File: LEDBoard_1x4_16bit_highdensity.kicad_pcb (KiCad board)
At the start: 2 copper layers, 16 x 14 mm, 10 parts, among them J1 signal_in, J2 signal_out, J3 power, U1 TLC5971PWP

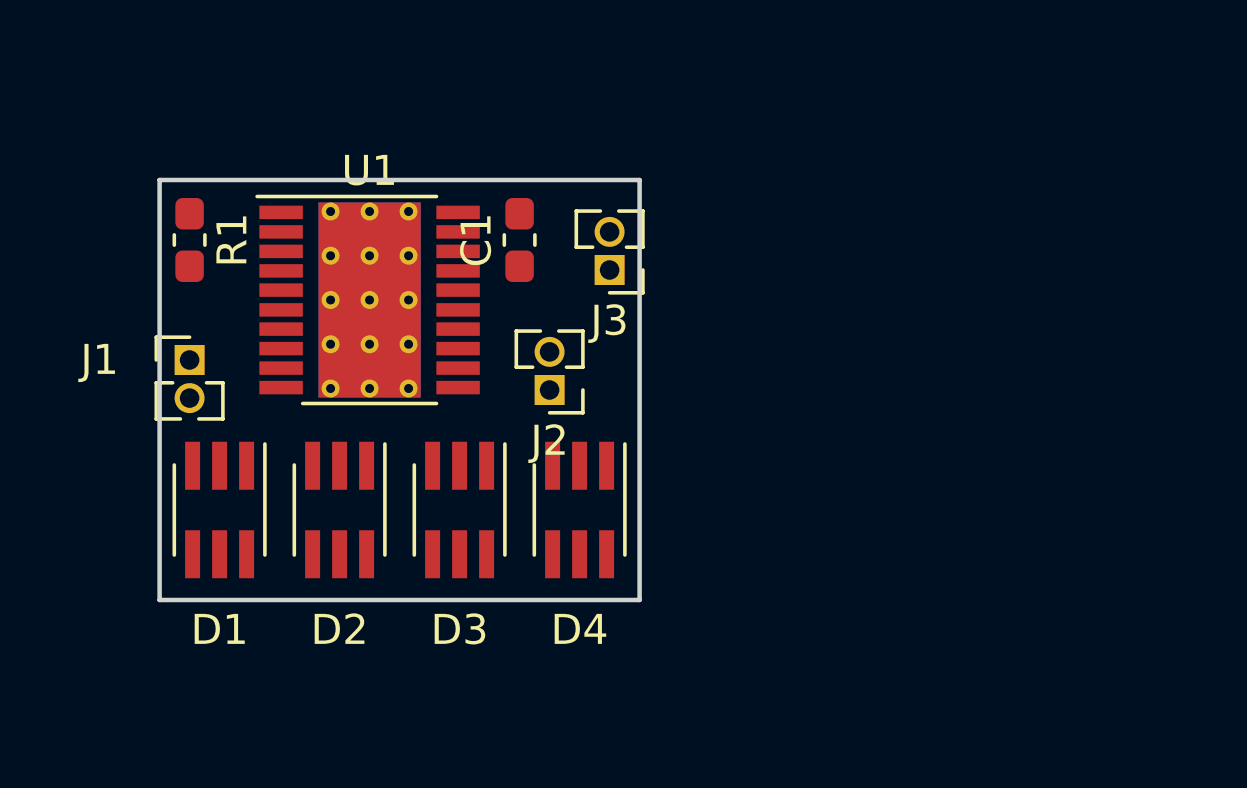
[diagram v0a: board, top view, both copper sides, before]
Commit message: basic component placement done
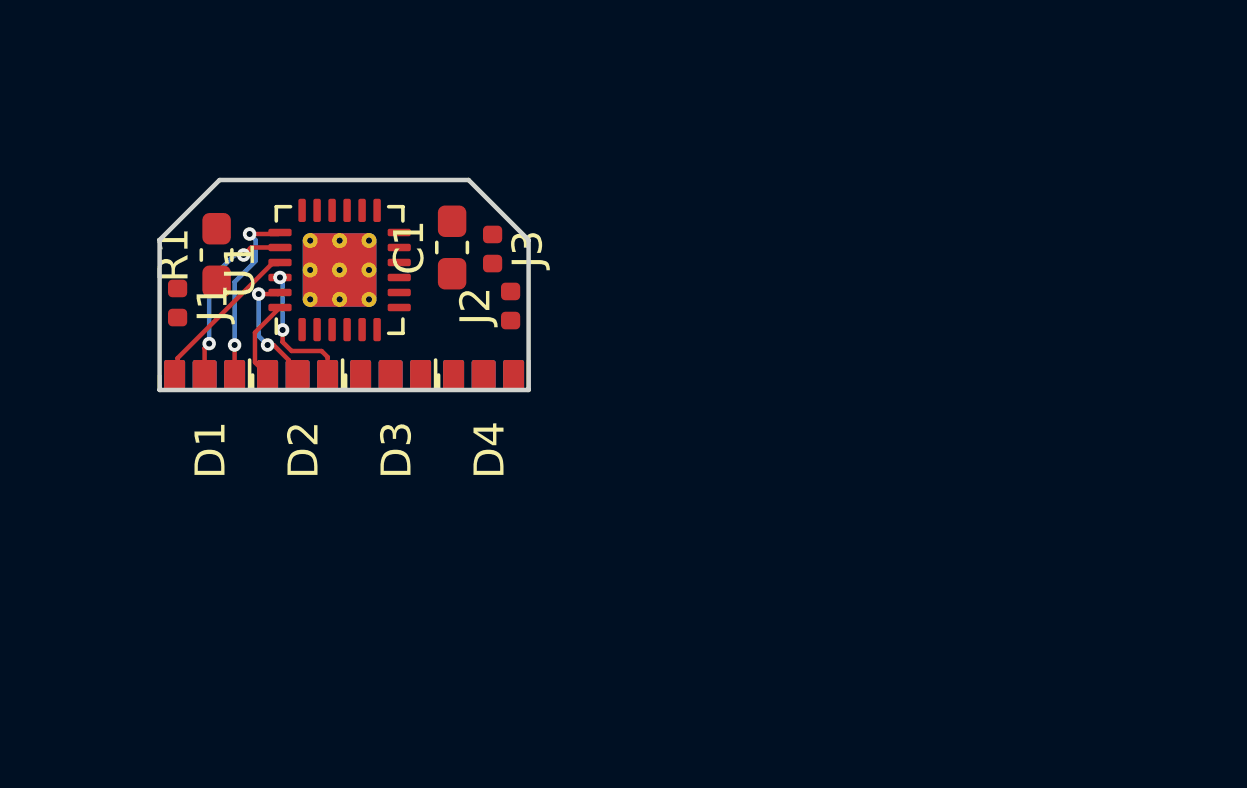
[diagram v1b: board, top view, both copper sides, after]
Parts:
- D1, D2, D3, D4: footprint LED_SMD:LED_Avago_PLCC6_3x2.8mm -> LEDs_SMD_NICHIA:LED_NSSM124_PCBEdge
- J1, J2, J3: footprint Connector_PinHeader_1.27mm:PinHeader_1x02_P1.27mm_Vertical -> Resistor_SMD:R_0402_1005Metric
- U1: footprint Package_SO:HTSSOP-20-1EP_4.4x6.5mm_P0.65mm_EP3.4x6.5mm_ThermalVias -> Package_DFN_QFN:VQFN-24-1EP_4x4mm_P0.5mm_EP2.45x2.45mm_ThermalVias
- moved D4 5.12 mm to (110.8, 107.0)
- moved D3 4.61 mm to (107.7, 107.0)
- moved D2 4.24 mm to (104.6, 107.0)
- moved D1 4.03 mm to (101.5, 107.0)
- moved J3 3.96 mm to (111.1, 102.3), turned to 270 degrees
- moved J2 3.09 mm to (111.7, 104.2), turned to 90 degrees
- moved C1 2.26 mm to (109.8, 102.2)
- moved J1 1.94 mm to (100.6, 104.1), turned to 270 degrees
- moved U1 1.41 mm to (106.0, 103.0), turned to 90 degrees
- moved R1 1.03 mm to (101.9, 102.5), turned to 90 degrees
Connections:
- U1 pad 1: Net-(R1-Pad1) -> /data_in
- U1 pad 10: /clock_in -> /led_3_r
- U1 pad 11: /clock_out -> /led_3_g
- U1 pad 12: /data_out -> /led_3_b
- U1 pad 13: /led_2_r -> VCC
- U1 pad 14: /led_2_g -> Net-(U1-Pad14)
- U1 pad 15: /led_2_b -> VCC
- U1 pad 16: /led_3_r -> Net-(R1-Pad1)
- U1 pad 17: /led_3_g -> Net-(U1-Pad17)
- U1 pad 18: /led_3_b -> GND
- U1 pad 19: VCC -> /led_0_r
- U1 pad 2: GND -> /clock_in
- U1 pad 20: VCC -> /led_0_g
- U1 pad 21: GND -> /led_0_b
- U1 pad 3: /led_0_r -> Net-(U1-Pad3)
- U1 pad 4: /led_0_g -> Net-(U1-Pad4)
- U1 pad 5: /led_0_b -> /clock_out
- U1 pad 6: /led_1_r -> /data_out
- U1 pad 7: /led_1_g -> /led_2_r
- U1 pad 8: /led_1_b -> /led_2_g
- U1 pad 9: /data_in -> /led_2_b
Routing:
- net /led_0_r: track 0.00 -> 6.11 mm, vias 0 -> 2
- net /led_0_g: track 0.00 -> 6.03 mm, vias 0 -> 2
- net /led_0_b: track 0.00 -> 5.34 mm
- net /led_1_r: track 0.00 -> 4.49 mm, vias 0 -> 2
- net /led_1_g: track 0.00 -> 4.08 mm, vias 0 -> 2
- net /led_1_b: track 0.00 -> 2.77 mm
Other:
- board size 16 x 14 mm -> 12.3 x 7 mm
- net class Default: clearance 0.2 -> 0.1; trace_width 0.25 -> 0.15; via_dia 0.8 -> 0.45; via_drill 0.4 -> 0.2
- rule pad_to_mask_clearance: 0.2 -> 0.075
- rule trace_clearance: 0.2 -> 0.1
- rule trace_min: 0.2 -> 0.1
- rule via_min_drill: 0.3 -> 0.2
- rule via_min_size: 0.4 -> 0.45

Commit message: placing & layout done :-)
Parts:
- U1: footprint Package_DFN_QFN:VQFN-24-1EP_4x4mm_P0.5mm_EP2.45x2.45mm_ThermalVias -> Package_SO:HTSSOP-20-1EP_4.4x6.5mm_P0.65mm_EP3.4x6.5mm_ThermalVias
- moved J3 3.55 mm to (111.7, 105.8)
- moved J1 2.10 mm to (100.6, 106.2)
- moved D1 2.00 mm to (101.5, 109.0)
- moved D2 2.00 mm to (104.6, 109.0)
- moved D3 2.00 mm to (107.7, 109.0)
- moved D4 2.00 mm to (110.8, 109.0)
- moved J2 1.89 mm to (110.7, 105.8)
- moved C1 1.57 mm to (111.0, 103.2), turned to 270 degrees
- moved R1 1.13 mm to (101.1, 103.3), turned to 270 degrees
- moved U1 0.61 mm to (106.1, 103.6), turned to 0 degrees
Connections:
- U1 pad 1: /data_in -> Net-(R1-Pad1)
- U1 pad 10: /led_3_r -> /clock_in
- U1 pad 11: /led_3_g -> /clock_out
- U1 pad 12: /led_3_b -> /data_out
- U1 pad 13: VCC -> /led_2_r
- U1 pad 14: Net-(U1-Pad14) -> /led_2_g
- U1 pad 15: VCC -> /led_2_b
- U1 pad 16: Net-(R1-Pad1) -> /led_3_r
- U1 pad 17: Net-(U1-Pad17) -> /led_3_g
- U1 pad 18: GND -> /led_3_b
- U1 pad 19: /led_0_r -> VCC
- U1 pad 2: /clock_in -> GND
- U1 pad 20: /led_0_g -> VCC
- U1 pad 21: /led_0_b -> GND
- U1 pad 3: Net-(U1-Pad3) -> /led_0_r
- U1 pad 4: Net-(U1-Pad4) -> /led_0_g
- U1 pad 5: /clock_out -> /led_0_b
- U1 pad 6: /data_out -> /led_1_r
- U1 pad 7: /led_2_r -> /led_1_g
- U1 pad 8: /led_2_g -> /led_1_b
- U1 pad 9: /led_2_b -> /data_in
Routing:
- net VCC: track 0.00 -> 22.7 mm, vias 0 -> 2
- net GND: track 0.00 -> 13.6 mm, vias 0 -> 1
- net /led_3_b: track 0.00 -> 8.27 mm, vias 0 -> 2
- net /led_3_r: track 0.00 -> 7.76 mm, vias 0 -> 2
- net /led_3_g: track 0.00 -> 6.59 mm, vias 0 -> 2
- net /led_2_b: track 0.00 -> 6.01 mm, vias 0 -> 2
- net /led_2_g: track 0.00 -> 4.75 mm, vias 0 -> 2
- net /led_2_r: track 0.00 -> 3.47 mm, vias 0 -> 2
- net Net-(R1-Pad1): track 0.00 -> 3.31 mm
- net /clock_in: track 0.00 -> 2.80 mm
- net /data_in: track 0.00 -> 2.63 mm
- net /led_0_b: track 5.34 -> 7.54 mm, vias 0 -> 2
- net /led_1_r: track 4.49 -> 6.40 mm
- net /data_out: track 0.00 -> 1.88 mm
- net /led_0_r: track 6.11 -> 7.91 mm
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- added copper zone on B.Cu, net GND
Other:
- board size 12.3 x 7 mm -> 12.3 x 9 mm
- board text added: "LEDs are Edge-Mounted"

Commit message: first placement test
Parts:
- D1, D2, D3, D4: footprint LEDs_SMD_NICHIA:LED_NSSM124_PCBEdge -> LEDs_SMD_NICHIA:LED_NSSM124_wViaHeatSinkBig_roundedPads
- U1: footprint Package_SO:HTSSOP-20-1EP_4.4x6.5mm_P0.65mm_EP3.4x6.5mm_ThermalVias -> Package_SO_mod:HTSSOP-20-1EP_4.4x6.5mm_P0.65mm_EP3.4x6.5mm_Mask2.75x3.43mm_ThermalVias_HandSolder
- moved J2 8.30 mm to (119.0, 106.0)
- moved J3 7.82 mm to (119.0, 103.0)
- moved D4 6.36 mm to (107.6, 114.5), turned to 180 degrees
- moved D2 5.53 mm to (104.0, 114.5), turned to 0 degrees
- moved C1 5.46 mm to (106.0, 101.0), turned to 180 degrees
- moved J1 3.60 mm to (97.0, 106.2)
- moved R1 2.69 mm to (102.5, 101.0), turned to 0 degrees
- moved D3 2.56 mm to (106.1, 111.0), turned to 180 degrees
- moved U1 2.56 mm to (104.5, 105.6)
- moved D1 2.24 mm to (102.5, 111.0), turned to 0 degrees
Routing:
- net VCC: track 22.7 -> 0.00 mm, vias 2 -> 0
- net GND: track 13.6 -> 0.00 mm, vias 1 -> 0
- net /led_3_b: track 8.27 -> 0.00 mm, vias 2 -> 0
- net /led_0_r: track 7.91 -> 0.00 mm, vias 2 -> 0
- net /led_3_r: track 7.76 -> 0.00 mm, vias 2 -> 0
- net /led_0_b: track 7.54 -> 0.00 mm, vias 2 -> 0
- net /led_0_g: track 6.85 -> 0.00 mm, vias 2 -> 0
- net /led_3_g: track 6.59 -> 0.00 mm, vias 2 -> 0
- net /led_1_r: track 6.40 -> 0.00 mm, vias 2 -> 0
- net /led_2_b: track 6.01 -> 0.00 mm, vias 2 -> 0
- net /led_2_g: track 4.75 -> 0.00 mm, vias 2 -> 0
- net /led_1_g: track 4.72 -> 0.00 mm, vias 2 -> 0
- net /led_1_b: track 3.47 -> 0.00 mm, vias 2 -> 0
- net /led_2_r: track 3.47 -> 0.00 mm, vias 2 -> 0
- net Net-(R1-Pad1): track 3.31 -> 0.00 mm
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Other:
- board size 12.3 x 9 mm -> 10 x 16.5 mm
- board text removed: "LEDs are Edge-Mounted"

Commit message: prepared amulet version
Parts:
- D1, D2, D3, D4: footprint LEDs_SMD_NICHIA:LED_NSSM124_wViaHeatSinkBig_roundedPads -> LEDs_SMD_NICHIA:LED_NSSM124
- U1: footprint Package_SO_mod:HTSSOP-20-1EP_4.4x6.5mm_P0.65mm_EP3.4x6.5mm_Mask2.75x3.43mm_ThermalVias_HandSolder -> Package_DFN_QFN:Texas_RGE0024H_EP2.7x2.7mm_ThermalVias
- moved J1 32.5 mm to (129.0, 112.0)
- moved J3 13.0 mm to (132.0, 103.0)
- moved D2 10.7 mm to (106.0, 104.0), turned to 270 degrees
- moved C1 10.6 mm to (113.0, 109.0)
- moved R1 10.5 mm to (113.0, 101.0)
- moved D1 9.01 mm to (102.0, 102.0), turned to 270 degrees
- moved D4 6.69 mm to (106.0, 108.0), turned to 90 degrees
- moved U1 6.53 mm to (111.0, 105.0)
- moved D3 6.47 mm to (102.0, 106.0), turned to 90 degrees
- moved J2 2.00 mm to (119.0, 108.0)
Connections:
- U1 pad 1: Net-(R1-Pad1) -> /data_in
- U1 pad 10: /clock_in -> /led_3_r
- U1 pad 11: /clock_out -> /led_3_g
- U1 pad 12: /data_out -> /led_3_b
- U1 pad 13: /led_2_r -> VCC
- U1 pad 14: /led_2_g -> Net-(U1-Pad14)
- U1 pad 15: /led_2_b -> VCC
- U1 pad 16: /led_3_r -> Net-(R1-Pad1)
- U1 pad 17: /led_3_g -> Net-(U1-Pad17)
- U1 pad 18: /led_3_b -> GND
- U1 pad 19: VCC -> /led_0_r
- U1 pad 2: GND -> /clock_in
- U1 pad 20: VCC -> /led_0_g
- U1 pad 21: GND -> /led_0_b
- U1 pad 3: /led_0_r -> Net-(U1-Pad3)
- U1 pad 4: /led_0_g -> Net-(U1-Pad4)
- U1 pad 5: /led_0_b -> /data_out
- U1 pad 6: /led_1_r -> /clock_out
- U1 pad 7: /led_1_g -> /led_2_r
- U1 pad 8: /led_1_b -> /led_2_g
- U1 pad 9: /data_in -> /led_2_b
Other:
- board size 10 x 16.5 mm -> 15 x 10 mm
